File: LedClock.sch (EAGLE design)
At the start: 2 parts, among them IC1 4511N, IC2 4051N

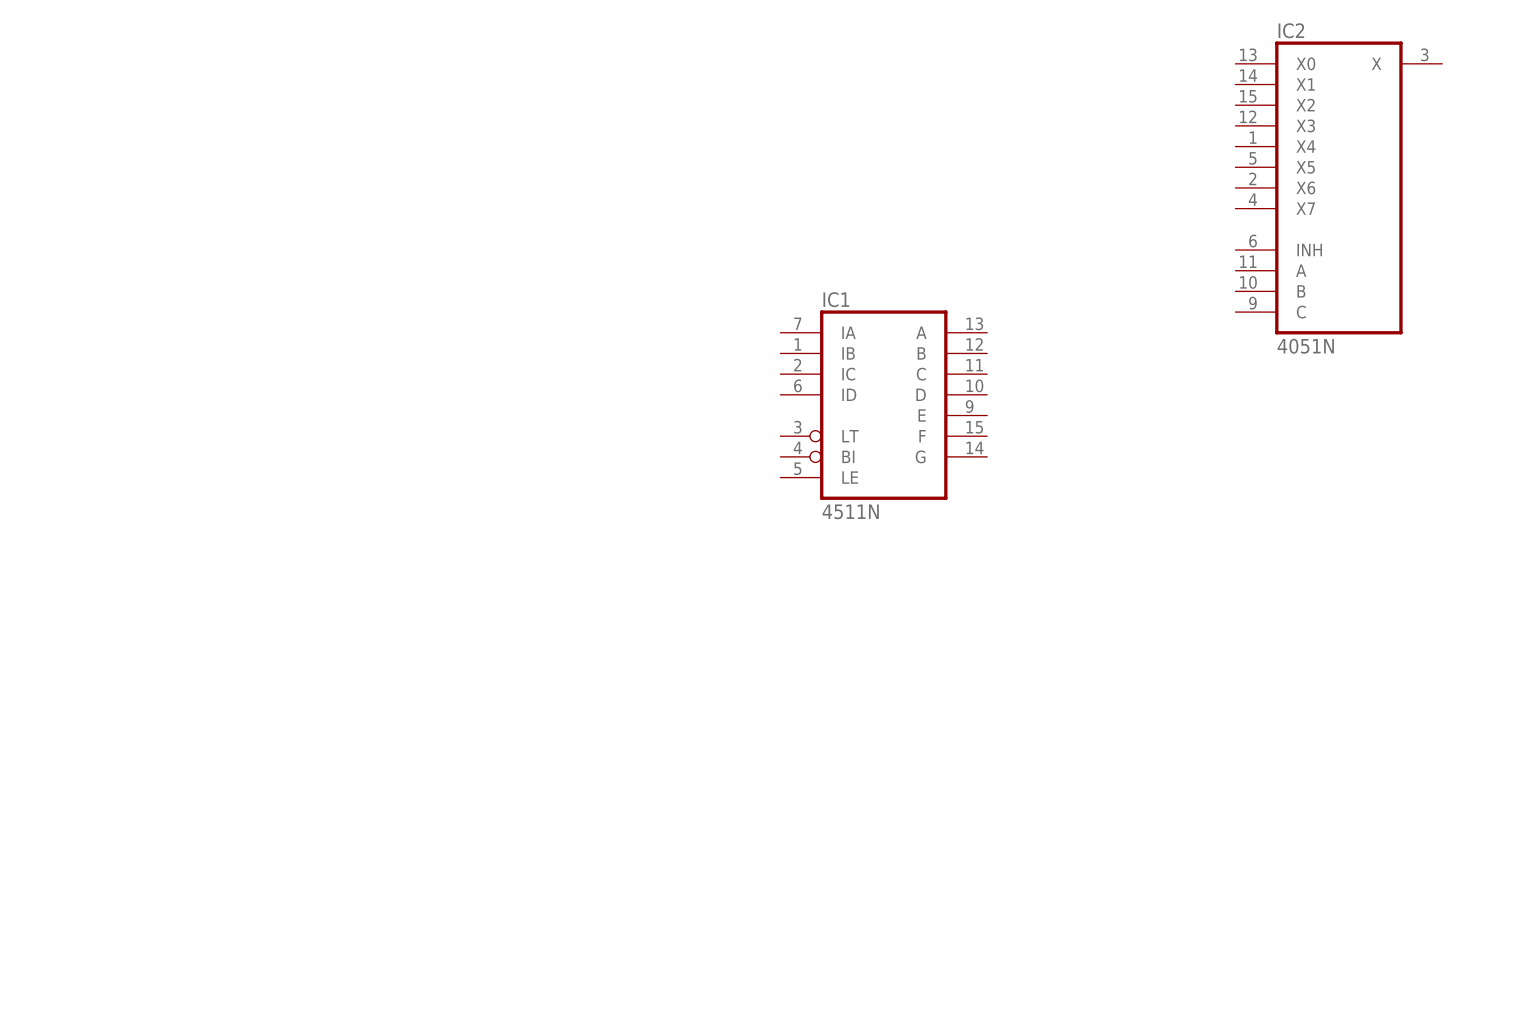
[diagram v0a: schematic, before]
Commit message: Adding components to schematic
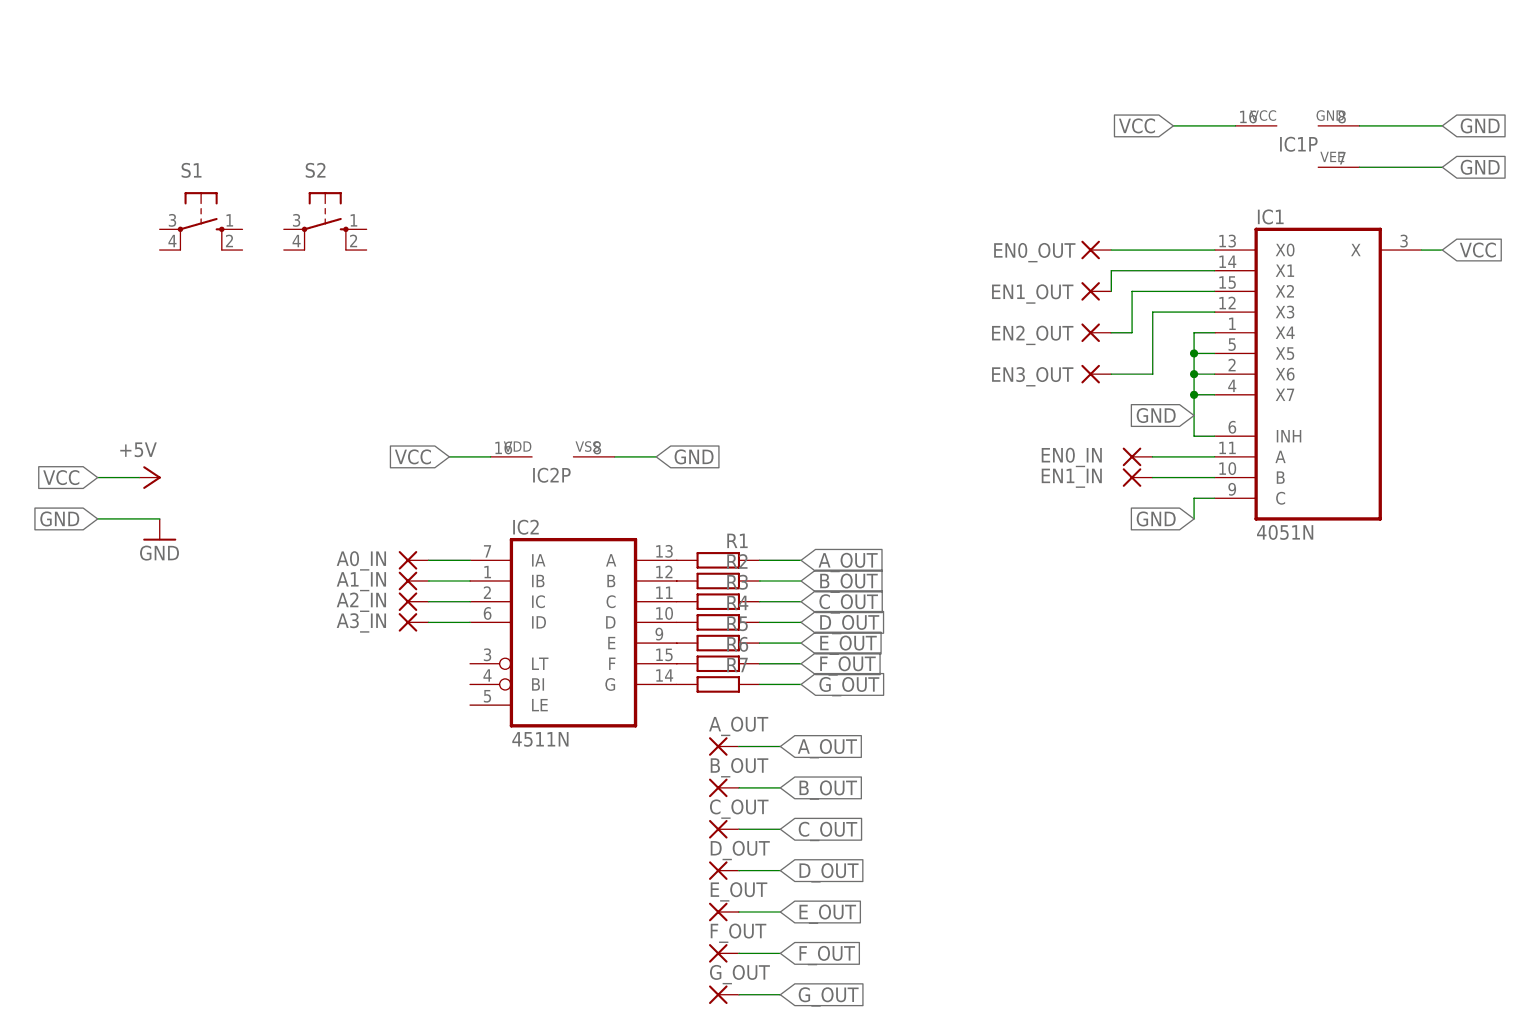
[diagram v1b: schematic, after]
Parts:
- added A0_IN, A1_IN, A2_IN, A3_IN, A_OUT, B_OUT, C_OUT, D_OUT, EN0_IN, EN0_OUT, EN1_IN, EN1_OUT, EN2_OUT, EN3_OUT, E_OUT, F_OUT, G_OUT: (no value), wirepad:2,54/1,0
- added R1, R2, R3, R4, R5, R6, R7: (no value), rcl:R-EU_M1206
- added S1, S2: (no value), switch-omron:10-XX
- IC1: value 4511N -> 4051N; device 45xx:4511N -> 40xx:4051N
- IC2: value 4051N -> 4511N; device 40xx:4051N -> 45xx:4511N
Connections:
- new net A_OUT: A_OUT.P, R1.1
- new net B_OUT: B_OUT.P, R2.1
- new net C_OUT: C_OUT.P, R3.1
- new net D_OUT: D_OUT.P, R4.1
- new net E_OUT: E_OUT.P, R5.1
- new net F_OUT: F_OUT.P, R6.1
- new net GND: IC1A.C, IC1A.INH, IC1A.X4, IC1A.X5, IC1A.X6, IC1A.X7, IC1P.GND, IC1P.VEE, IC2P.VSS
- new net G_OUT: G_OUT.P, R7.1
- new net N$1: IC2A.A, R1.2
- new net N$10: EN0_IN.P, IC1A.A
- new net N$11: EN1_IN.P, IC1A.B
- new net N$12: EN2_OUT.P, IC1A.X2
- new net N$13: EN3_OUT.P, IC1A.X3
- new net N$14: A0_IN.P, IC2A.IA
- new net N$15: A1_IN.P, IC2A.IB
- new net N$16: A2_IN.P, IC2A.IC
- new net N$17: A3_IN.P, IC2A.ID
- new net N$2: IC2A.B, R2.2
- new net N$3: IC2A.C, R3.2
- new net N$4: IC2A.D, R4.2
- new net N$5: IC2A.E, R5.2
- new net N$6: IC2A.F, R6.2
- new net N$7: IC2A.G, R7.2
- new net N$8: EN0_OUT.P, IC1A.X0
- new net N$9: EN1_OUT.P, IC1A.X1
- new net VCC: IC1A.X, IC1P.VCC, IC2P.VDD

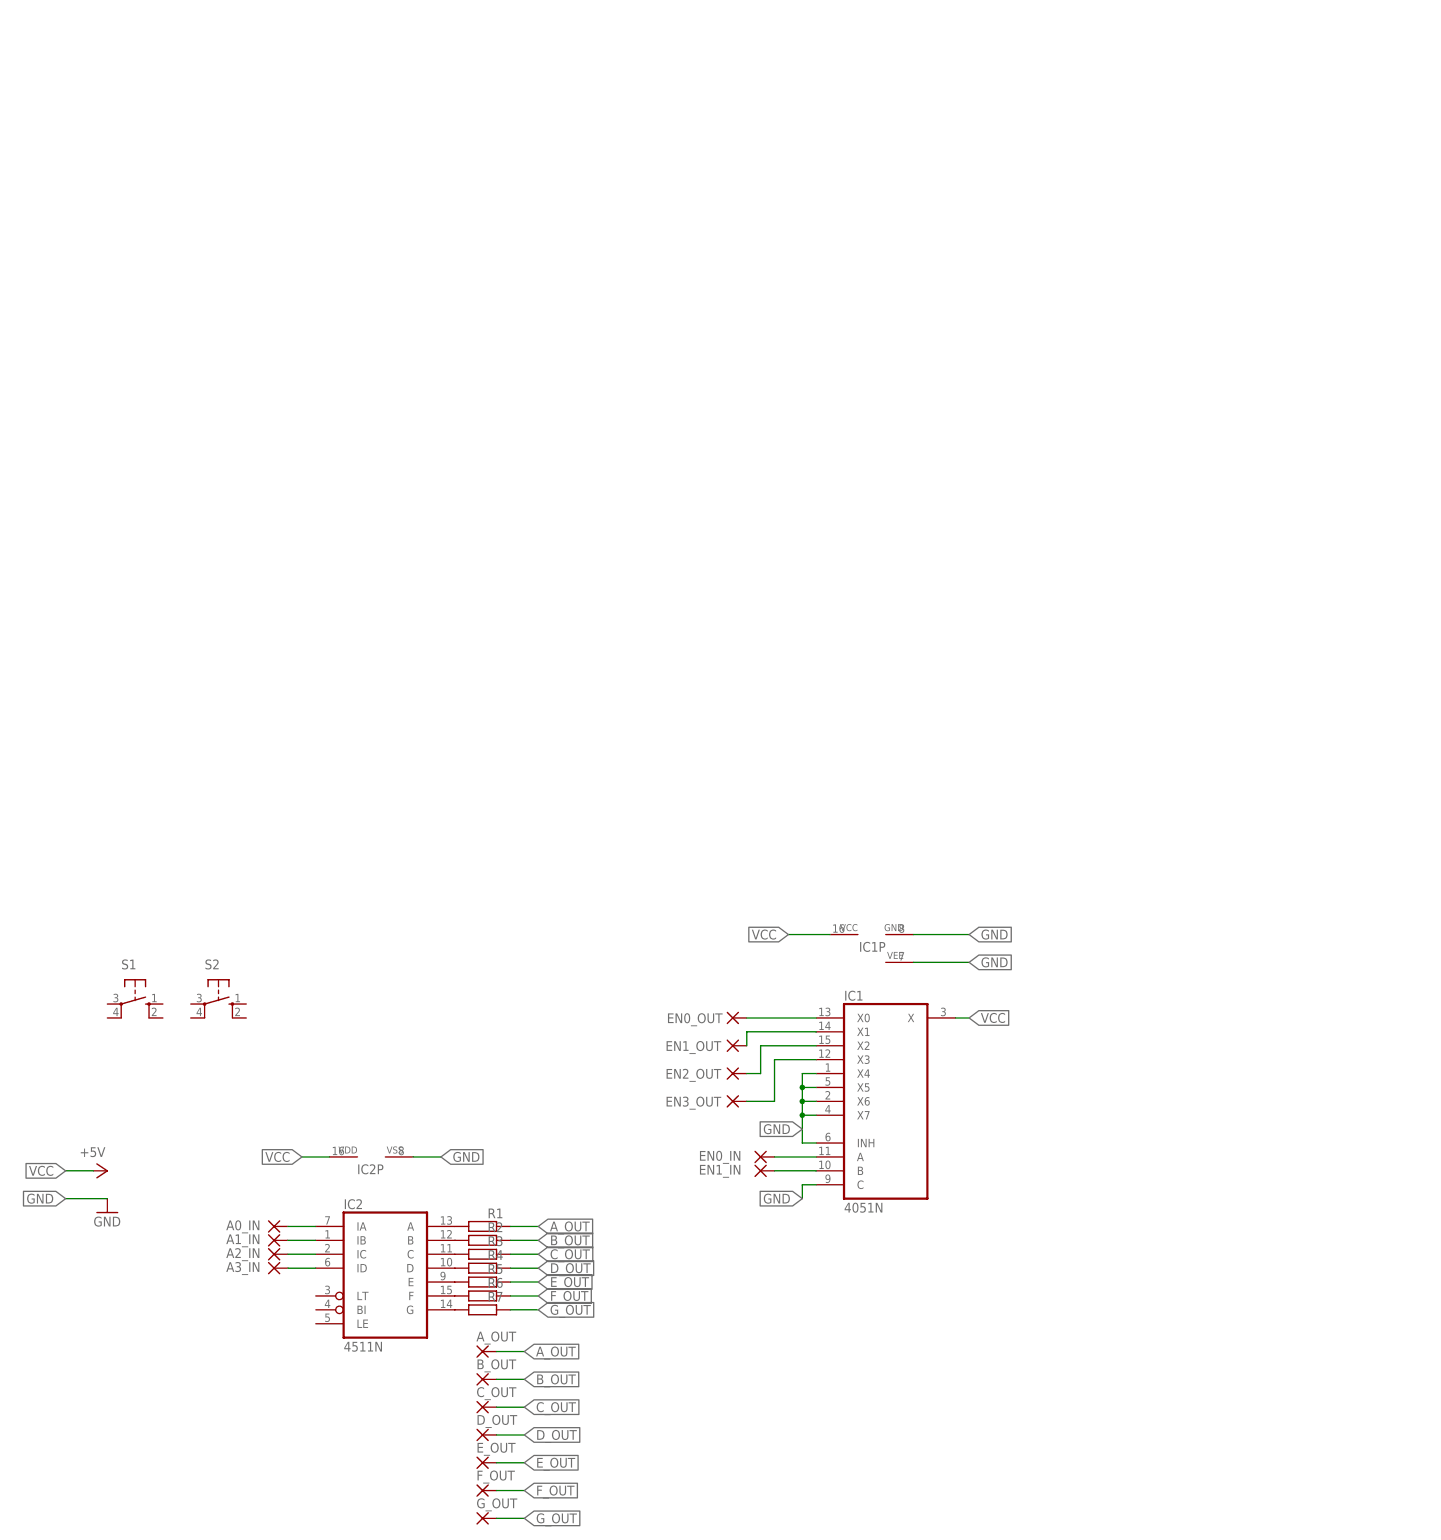
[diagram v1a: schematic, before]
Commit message: schematic v0. All parts are added.
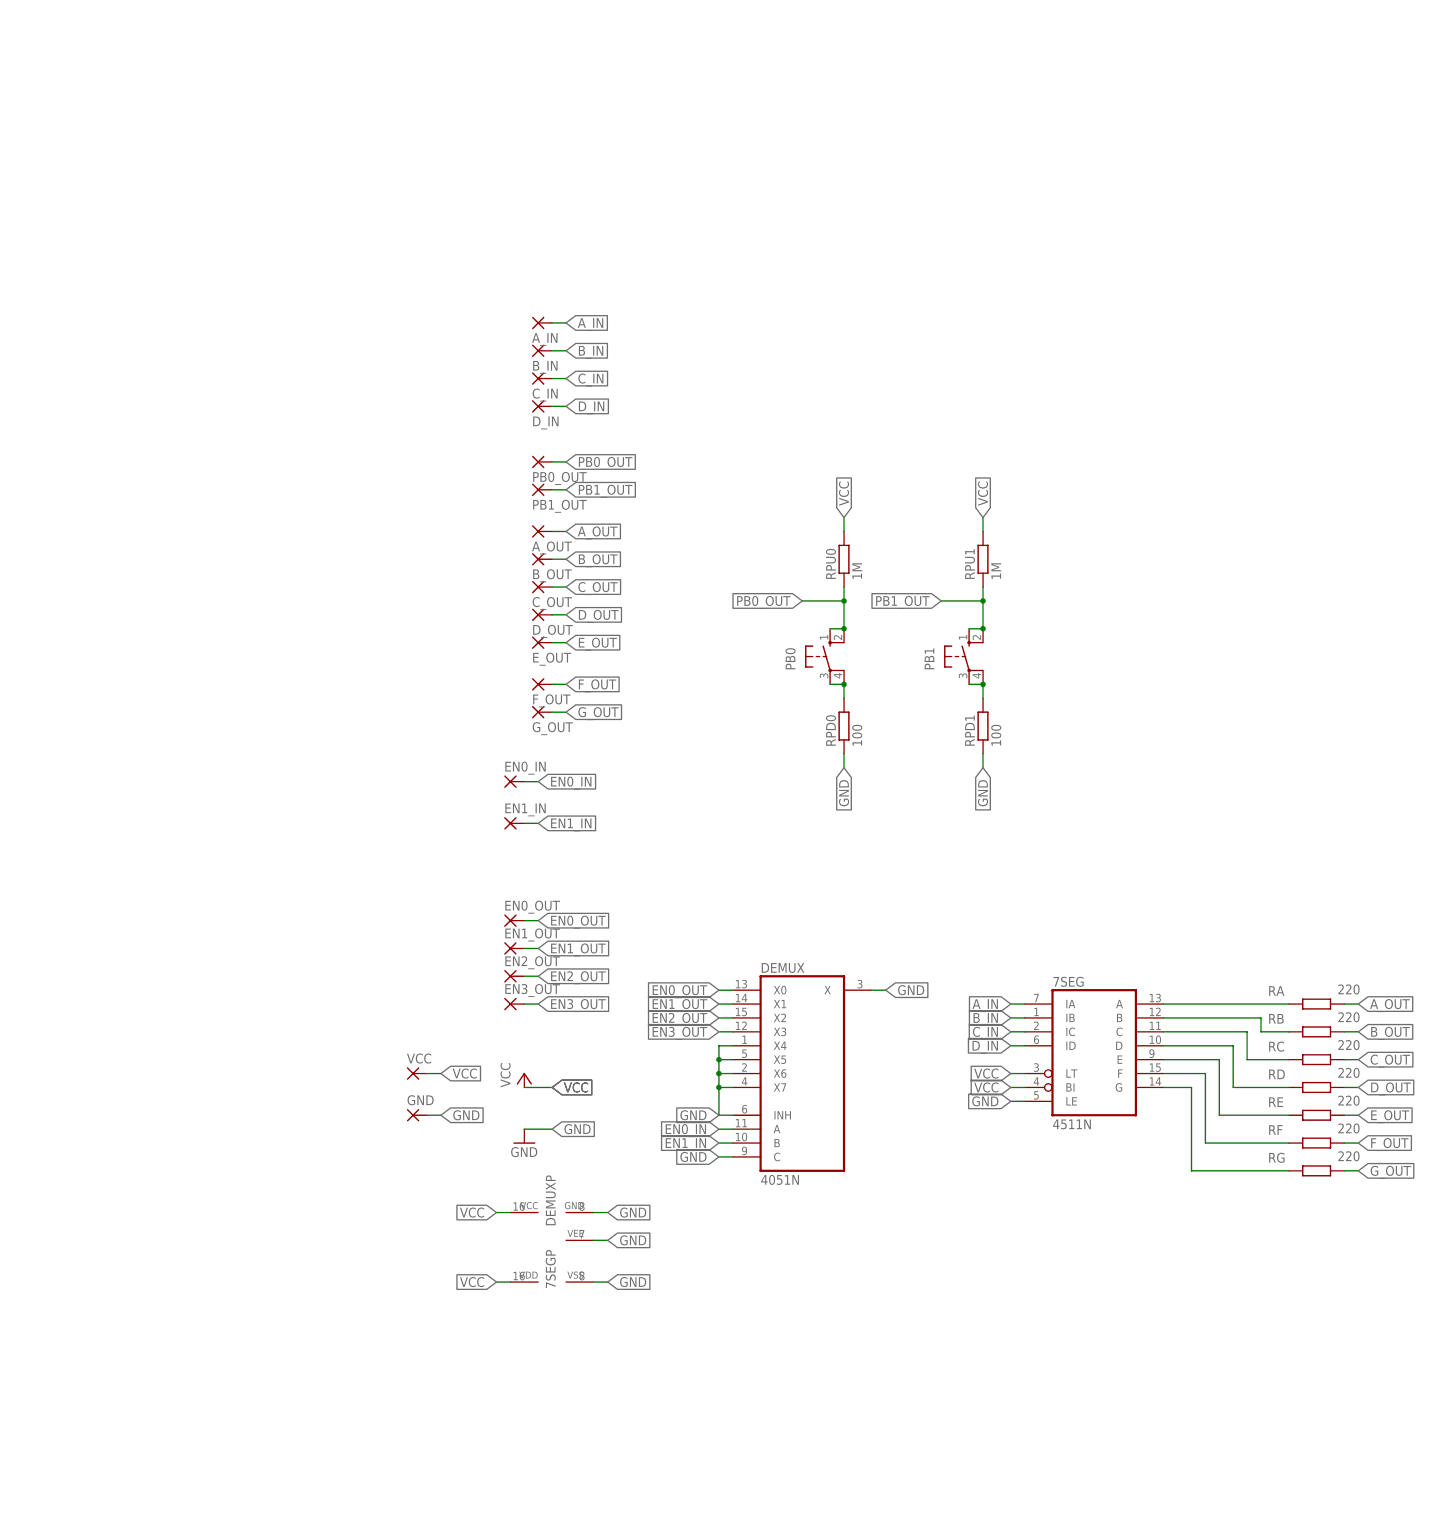
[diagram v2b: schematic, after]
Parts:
- removed A0_IN, A1_IN, A2_IN, A3_IN: (no value), wirepad:2,54/1,0
- removed IC1: 4051N, 40xx:4051N
- removed IC2: 4511N, 45xx:4511N
- removed R1, R2, R3, R4, R5, R6, R7: (no value), rcl:R-EU_M1206
- removed S1, S2: (no value), switch-omron:10-XX
- added 7SEG: 4511N, 45xx:4511N
- added A_IN, B_IN, C_IN, D_IN, GND, PB0_OUT, PB1_OUT, VCC: (no value), wirepad:2,54/1,0
- added DEMUX: 4051N, 40xx:4051N
- added PB0, PB1: (no value), switch-omron:10-XX
- added RA, RB, RC, RD, RE, RF, RG: 220, rcl:R-EU_R1206
- added RPD0, RPD1: 100, rcl:R-EU_R1206
- added RPU0, RPU1: 1M, rcl:R-EU_R1206
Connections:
- removed net N$15: A1_IN.P, IC2A.IB
- removed net N$16: A2_IN.P, IC2A.IC
- removed net N$17: A3_IN.P, IC2A.ID
- removed net N$3: IC2A.C, R3.2
- removed net N$4: IC2A.D, R4.2
- removed net N$5: IC2A.E, R5.2
- removed net N$6: IC2A.F, R6.2
- removed net N$7: IC2A.G, R7.2
- new net A_IN: 7SEGA.IA, A_IN.P
- new net B_IN: 7SEGA.IB, B_IN.P
- new net C_IN: 7SEGA.IC, C_IN.P
- new net D_IN: 7SEGA.ID, D_IN.P
- new net EN0_IN: DEMUXA.A, EN0_IN.P
- new net EN0_OUT: DEMUXA.X0, EN0_OUT.P
- new net EN1_IN: DEMUXA.B, EN1_IN.P
- new net EN1_OUT: DEMUXA.X1, EN1_OUT.P
- new net EN2_OUT: DEMUXA.X2, EN2_OUT.P
- new net EN3_OUT: DEMUXA.X3, EN3_OUT.P
- new net PB0_OUT: PB0.S, PB0.S1, PB0_OUT.P, RPU0.1
- new net PB1_OUT: PB1.S, PB1.S1, PB1_OUT.P, RPU1.1
- net A_OUT: now also RA.2; no longer R1.1
- net B_OUT: now also RB.2; no longer R2.1
- net C_OUT: now also RC.2; no longer R3.1
- net D_OUT: now also RD.2; no longer R4.1
- net E_OUT: now also RE.2; no longer R5.1
- net F_OUT: now also RF.2; no longer R6.1
- net GND: now also 7SEGA.LE, 7SEGP.VSS, DEMUXA.C, DEMUXA.INH, DEMUXA.X, DEMUXA.X4, DEMUXA.X5, DEMUXA.X6, DEMUXA.X7, DEMUXP.GND, DEMUXP.VEE, GND.P, RPD0.1, RPD1.1; no longer IC1A.C, IC1A.INH, IC1A.X4, IC1A.X5, IC1A.X6, IC1A.X7, IC1P.GND, IC1P.VEE, IC2P.VSS
- net G_OUT: now also RG.2; no longer R7.1
- net N$1: now also PB1.P, PB1.P1, RPD1.2; no longer IC2A.A, R1.2
- net N$10: now also 7SEGA.C, RC.1; no longer EN0_IN.P, IC1A.A
- net N$11: now also 7SEGA.D, RD.1; no longer EN1_IN.P, IC1A.B
- net N$12: now also 7SEGA.E, RE.1; no longer EN2_OUT.P, IC1A.X2
- net N$13: now also 7SEGA.F, RF.1; no longer EN3_OUT.P, IC1A.X3
- net N$14: now also 7SEGA.G, RG.1; no longer A0_IN.P, IC2A.IA
- net N$2: now also PB0.P, PB0.P1, RPD0.2; no longer IC2A.B, R2.2
- net N$8: now also 7SEGA.A, RA.1; no longer EN0_OUT.P, IC1A.X0
- net N$9: now also 7SEGA.B, RB.1; no longer EN1_OUT.P, IC1A.X1
- net VCC: now also 7SEGA.BI, 7SEGA.LT, 7SEGP.VDD, DEMUXP.VCC, RPU0.2, RPU1.2, VCC.P; no longer IC1A.X, IC1P.VCC, IC2P.VDD
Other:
- moved on the sheet: A_OUT, B_OUT, C_OUT, D_OUT, EN0_IN, EN0_OUT, EN1_IN, EN1_OUT, EN2_OUT, EN3_OUT, E_OUT, F_OUT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

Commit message: All parts are added. schematic_V0
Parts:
- added LD0_A, LD0_C, LD1_A, LD1_C: (no value), wirepad:2,54/1,0
- added RA1, RA2: 680, rcl:R-EU_R1206
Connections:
- new net LD0_A: LD0_A.P, RA1.2
- new net LD1_A: LD1_A.P, RA2.2
- net GND: now also LD0_C.P, LD1_C.P
- net VCC: now also RA1.1, RA2.1
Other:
- note added: "PowerBlock"
- moved on the sheet: 7SEG, 7SEGP, A_IN, A_OUT, B_IN, B_OUT, C_IN, C_OUT, DEMUX, DEMUXP, D_IN, D_OUT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

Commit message: Add pcd design v0
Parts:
- renumbered RA1 to RLD1, RA2 to RLD2
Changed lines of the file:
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@@
 <part name="LD0_A" library="wirepad" deviceset="2,54/1,0" device=""/>
 <part name="LD1_A" library="wirepad" deviceset="2,54/1,0" device=""/>
-<part name="RA1" library="rcl" deviceset="R-EU_" device="R1206" value="680"/>
-<part name="RA2" library="rcl" deviceset="R-EU_" device="R1206" value="680"/>
+<part name="RLD1" library="rcl" deviceset="R-EU_" device="R1206" value="680"/>
+<part name="RLD2" library="rcl" deviceset="R-EU_" device="R1206" value="680"/>
 <part name="LD0_C" library="wirepad" deviceset="2,54/1,0" device=""/>
 <part name="LD1_C" library="wirepad" deviceset="2,54/1,0" device=""/>
@@
 <attribute name="VALUE" x="-11.303" y="75.438" size="1.778" layer="96"/>
 </instance>
-<instance part="RA1" gate="G$1" x="93.98" y="200.66" smashed="yes">
+<instance part="RLD1" gate="G$1" x="93.98" y="200.66" smashed="yes">
 <attribute name="NAME" x="85.09" y="202.1586" size="1.778" layer="95"/>
 <attribute name="VALUE" x="97.79" y="202.438" size="1.778" layer="96"/>
 </instance>
-<instance part="RA2" gate="G$1" x="93.98" y="193.04" smashed="yes">
+<instance part="RLD2" gate="G$1" x="93.98" y="193.04" smashed="yes">
 <attribute name="NAME" x="85.09" y="194.5386" size="1.778" layer="95"/>
 <attribute name="VALUE" x="97.79" y="194.818" size="1.778" layer="96"/>
@@
 </segment>
 <segment>
-<pinref part="RA1" gate="G$1" pin="1"/>
+<pinref part="RLD1" gate="G$1" pin="1"/>
 <wire x1="88.9" y1="200.66" x2="86.36" y2="200.66" width="0.1524" layer="91"/>
 <label x="86.36" y="200.66" size="1.778" layer="95" rot="R180" xref="yes"/>
 </segment>
 <segment>
-<pinref part="RA2" gate="G$1" pin="1"/>
+<pinref part="RLD2" gate="G$1" pin="1"/>
 <wire x1="88.9" y1="193.04" x2="86.36" y2="193.04" width="0.1524" layer="91"/>
 <label x="86.36" y="193.04" size="1.778" layer="95" rot="R180" xref="yes"/>
@@
 <net name="LD0_A" class="0">
 <segment>
-<pinref part="RA1" gate="G$1" pin="2"/>
+<pinref part="RLD1" gate="G$1" pin="2"/>
 <wire x1="99.06" y1="200.66" x2="101.6" y2="200.66" width="0.1524" layer="91"/>
 <label x="101.6" y="200.66" size="1.778" layer="95" xref="yes"/>
@@
 <net name="LD1_A" class="0">
 <segment>
-<pinref part="RA2" gate="G$1" pin="2"/>
+<pinref part="RLD2" gate="G$1" pin="2"/>
 <wire x1="99.06" y1="193.04" x2="101.6" y2="193.04" width="0.1524" layer="91"/>
 <label x="101.6" y="193.04" size="1.778" layer="95" xref="yes"/>
